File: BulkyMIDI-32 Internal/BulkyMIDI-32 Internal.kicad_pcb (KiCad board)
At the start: 2 copper layers, 100 x 97.9 mm, 51 parts, among them J1 Front Panel, J10 INT_TRS_SWAP, J11 THRU_TRS_SWAP, J2 MIDI OUT, J3 EXT_MIDI, J4 AUDIO, J5 INT_MIDI, J6 SERIAL, J7 POWER, J8 THRU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

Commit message: Small changes to internal layout
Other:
- board text added: "BulkyMIDI-32 Internal (rev. B) github.com/tebl"
- board text removed: "BulkyMIDI-32 Internal (rev. A) github.com/tebl"
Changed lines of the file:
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@@
       (effects (font (size 1 1) (thickness 0.15)))
     )
-    (fp_text value 10nF (at 2.5 2.5) (layer F.Fab)
+    (fp_text value 10nF (at 2.5 -2.54) (layer F.SilkS)
       (effects (font (size 1 1) (thickness 0.15)))
     )
@@
   (gr_line (start 117.16688 150) (end 101.6 150) (layer Edge.Cuts) (width 0.05))
   (gr_line (start 101.6 52.1) (end 101.6 150) (layer Edge.Cuts) (width 0.05))
-  (gr_text "BulkyMIDI-32\nInternal (rev. A)\ngithub.com/tebl" (at 151.6 141.264) (layer B.SilkS)
+  (gr_text "BulkyMIDI-32\nInternal (rev. B)\ngithub.com/tebl" (at 151.6 141.264) (layer B.SilkS)
     (effects (font (size 1 1) (thickness 0.15)) (justify mirror))
   )

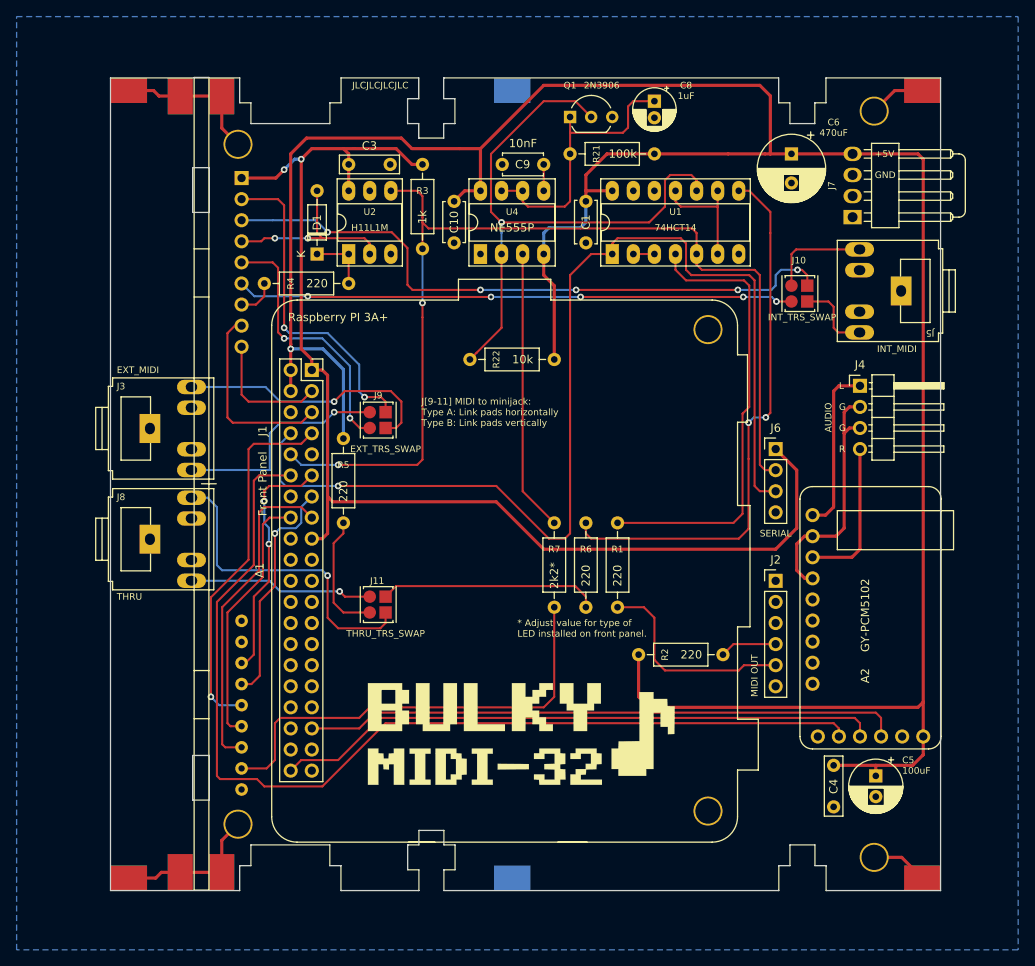
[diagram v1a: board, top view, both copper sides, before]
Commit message: Added little nubs to PJ-307 footprint
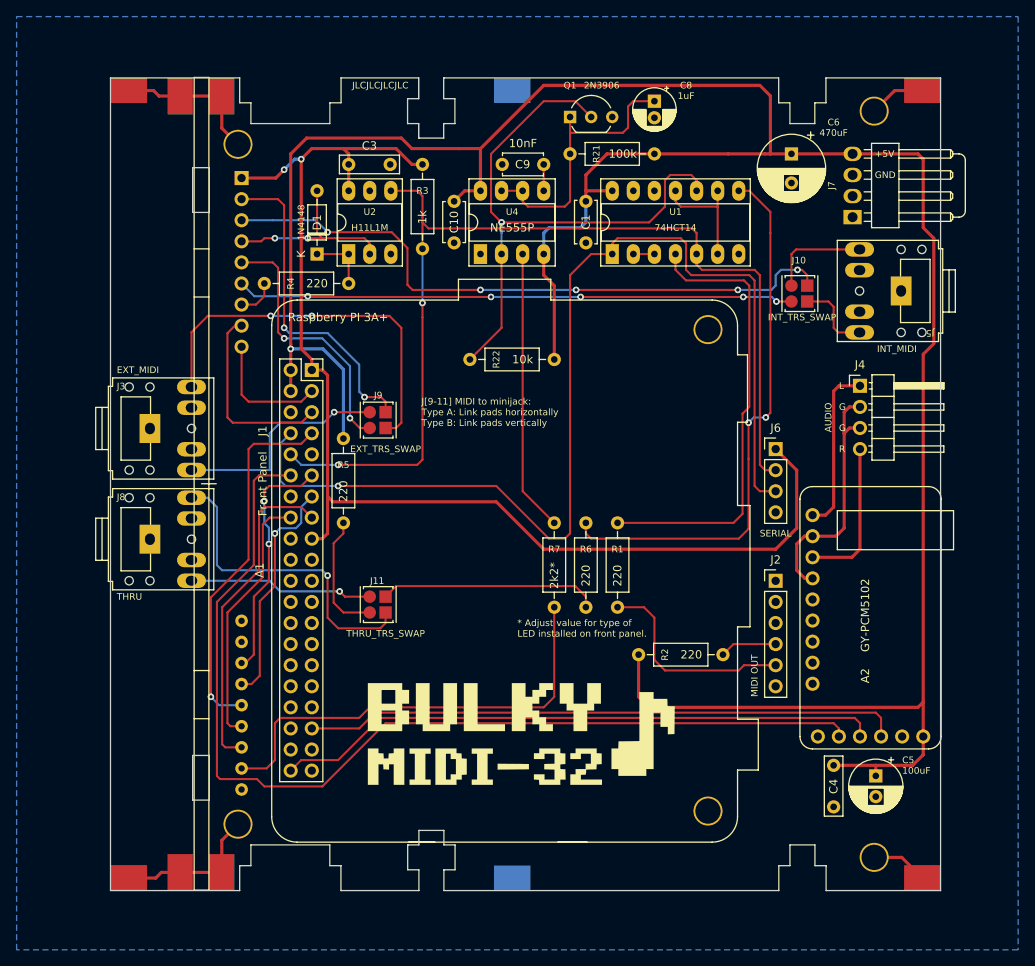
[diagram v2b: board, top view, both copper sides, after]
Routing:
- net Net-(J3-Pad2): track 31.8 -> 46.9 mm, vias 1 -> 2
- net +5V: track 319.5 -> 320.6 mm
